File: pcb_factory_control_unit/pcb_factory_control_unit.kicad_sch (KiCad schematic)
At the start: 45 parts, among them J1 STDC14, J2 Micro_SD_Card_Det1, SW1 Reset, SW2 Boot, U1 STM32H563VITx, U10 SIT3051TK

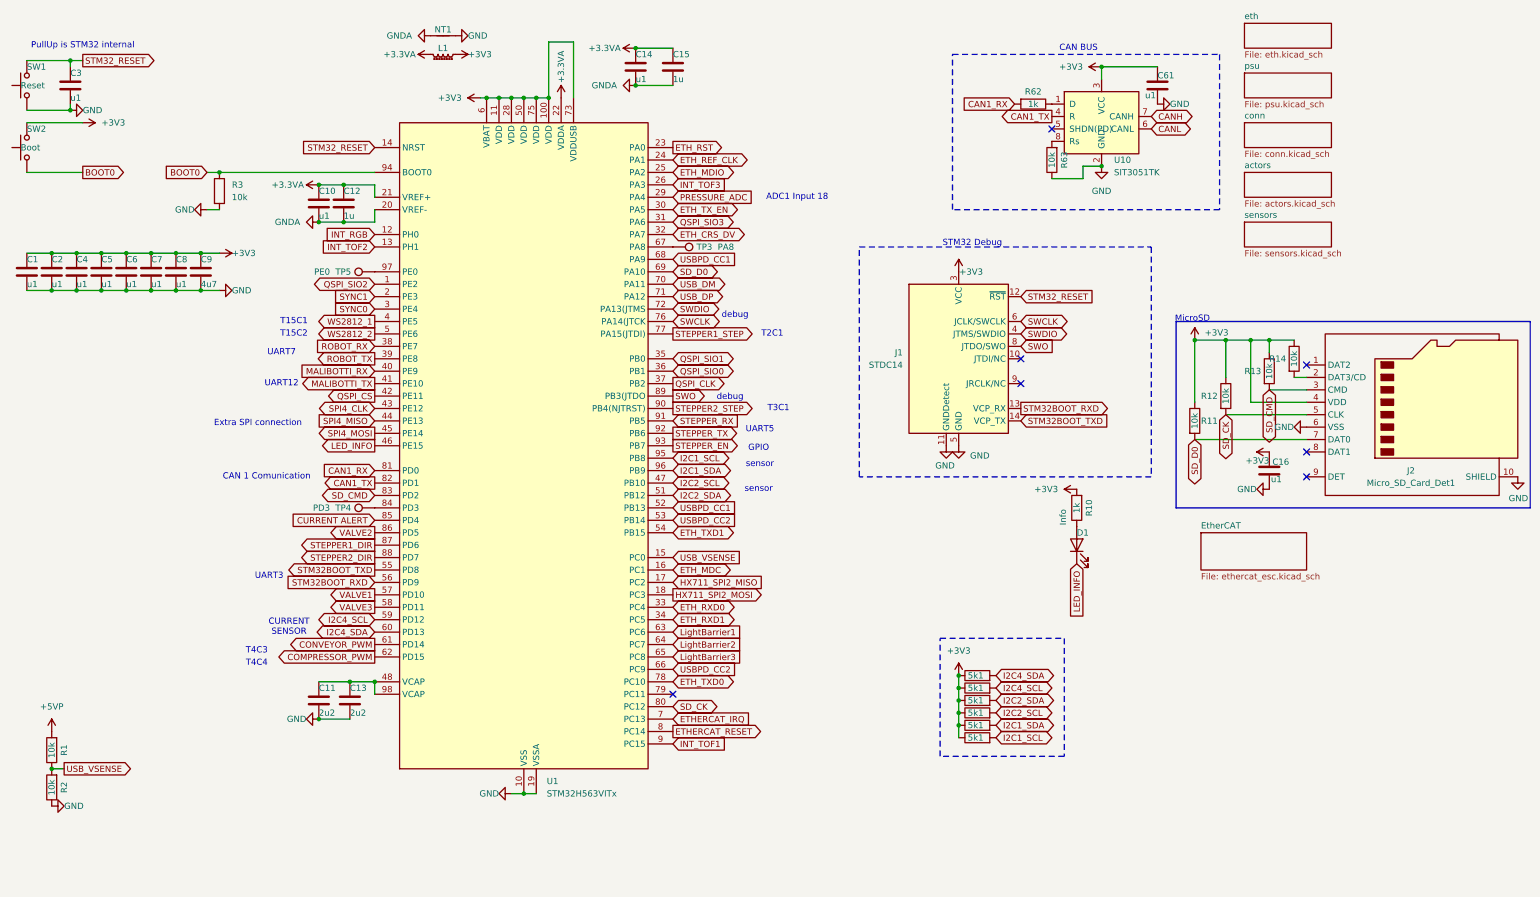
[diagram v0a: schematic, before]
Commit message: Improved Schematics EtherCAT after Claude-Session. Refactoring in Builder
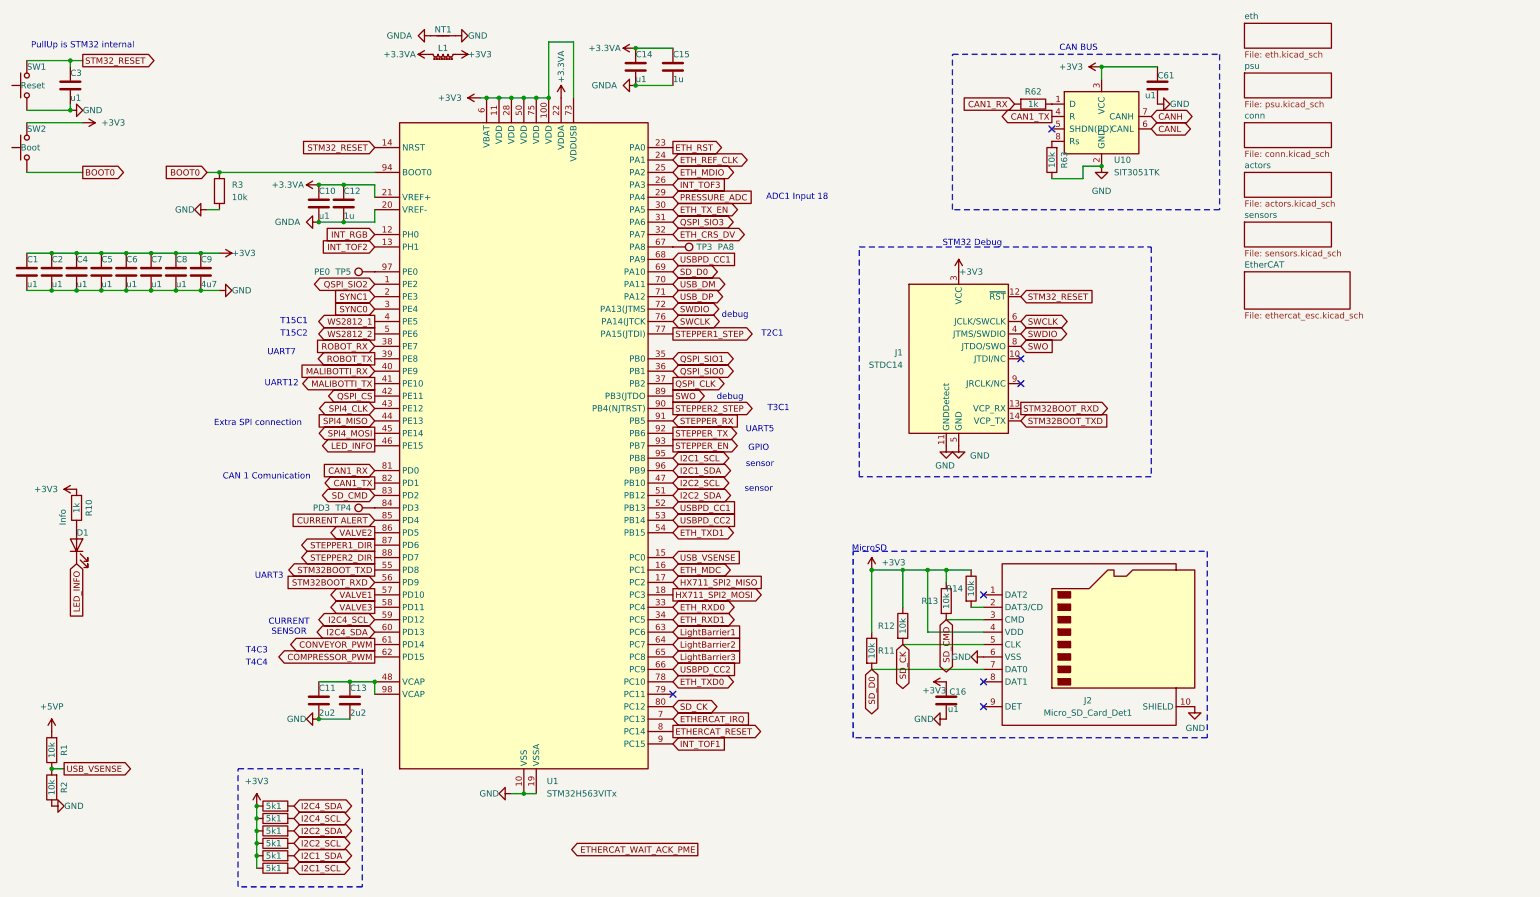
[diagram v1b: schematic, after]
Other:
- moved on the sheet: C16, D1, J2, R10, R11, R12, R13, R14

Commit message: Control Unit PCB: schematic rework (PSU, MX26631DL, XL6009 module, ERC fixes), new placement on 90 mm high board
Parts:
- added J1: CAN, liebler_CONN:JST_XH_B3B-XH-A_1x03_P2.50mm_Vertical_smaller, symbol Connector_Generic:Conn_01x03
- renumbered C8 to C10, C9 to C11, C10 to C12, C11 to C13, C12 to C14, C13 to C15, C61 to C17, C14 to C2, C2 to C3, C15 to C4, C3 to C5, C4 to C6, C5 to C7, C6 to C8, C7 to C9, J1 to J2, J2 to J3, R10 to R1, R3 to R10, R62 to R13, R13 to R14, R63 to R15, R14 to R16, R4 to R2, R5 to R3, R6 to R4, R7 to R5, R8 to R6, R9 to R7, R1 to R8, R2 to R9, TP5 to TP1, TP4 to TP2, U10 to U2
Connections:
- net CANH: now also J1.1 (Pin_1)
- net CANL: now also J1.3 (Pin_3)
- net GND: now also J3.SH (SHIELD), J1.2 (Pin_2); no longer J3.10 (SHIELD)
- net VACUUM_PUMP: now reaches U1.79 (PC11)
- net LightBarrier3: no longer names the net of U1.65 (PC8)
- no-connect marks 7 -> 6
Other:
- note added: "Hier war mal LightBarrier3"
- moved on the sheet: C16, C17, C2, C4, D1, J2, J3, R1, R11, R12, R13, R14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

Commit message: WIP PCB
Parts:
- removed TP1: PE0, TestPoint:TestPoint_THTPad_D1.0mm_Drill0.5mm, symbol Connector:TestPoint
- removed TP2: PD3, TestPoint:TestPoint_THTPad_D1.0mm_Drill0.5mm, symbol Connector:TestPoint
- removed TP3: PA8, TestPoint:TestPoint_THTPad_D1.0mm_Drill0.5mm, symbol Connector:TestPoint
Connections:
- net ETHERCAT_RESET: now also U1.84 (PD3); no longer U1.8 (PC14)
- net INT_TOF2: now also U1.46 (PE15); no longer U1.13 (PH1)
- net LED_INFO: no longer U1.46 (PE15)
- net LightBarrier1: now also U1.64 (PC7); no longer U1.63 (PC6)
- net LightBarrier2: now also U1.65 (PC8); no longer U1.64 (PC7)
- net VALVE1: now also U1.67 (PA8); no longer U1.57 (PD10)
- net VALVE2: now also U1.63 (PC6); no longer U1.86 (PD5)
- new net VACUUM_VALVE: U1.57 (PD10)
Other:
- note removed: "Hier war mal LightBarrier3"

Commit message: PCB WIP
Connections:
- net LED_INFO: now also U1.13 (PH1)
- net MALIBOTTI_RX: now also U1.38 (PE7); no longer U1.40 (PE9)
- net MALIBOTTI_TX: now also U1.39 (PE8); no longer U1.41 (PE10)
- net ROBOT_RX: now also U1.40 (PE9); no longer U1.38 (PE7)
- net ROBOT_TX: now also U1.41 (PE10); no longer U1.39 (PE8)

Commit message: wip
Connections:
- net CANH: now also J1.3 (Pin_3); no longer J1.1 (Pin_1)
- net CANL: now also J1.1 (Pin_1); no longer J1.3 (Pin_3)
- net MALIBOTTI_RX: now also U1.40 (PE9); no longer U1.38 (PE7)
- net MALIBOTTI_TX: now also U1.41 (PE10); no longer U1.39 (PE8)
- net ROBOT_RX: now also U1.38 (PE7); no longer U1.40 (PE9)
- net ROBOT_TX: now also U1.39 (PE8); no longer U1.41 (PE10)

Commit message: Step Up Converter
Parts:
- removed C10: u1, Capacitor_SMD:C_0402_1005Metric, symbol Device:C

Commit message: FCB ready for review
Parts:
- J1: value CAN -> CAN-Bus
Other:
- moved on the sheet: C11
